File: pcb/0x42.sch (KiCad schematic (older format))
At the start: 26 parts, among them J1 USB_C_Receptacle_USB2.0, J2 ISP, Q1 2N7002, SW1 ~Reset, U1 ATmega32U4-MU, U2 PRTR5V0U2X, Y1 Crystal_GND24

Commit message: IS31 Led matrix
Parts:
- removed Q1: 2N7002, Package_TO_SOT_SMD:SOT-23, symbol Transistor_FET:2N7002
- removed R8: 100, 0xLib_Passive_SMD:R_0603_1608Metric, symbol Device:R
- removed R9: 10k, 0xLib_Passive_SMD:R_0603_1608Metric, symbol Device:R
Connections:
- net labels added: SCL, SDA
- net labels removed: LED_GND, LED_PWM
- wire segments 172 -> 164
- no-connect marks 8 -> 7
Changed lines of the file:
@@
 F1 "leds.sch" 50
 F2 "LED_DIN" I L 8900 3950 50
-F3 "LED_GND" I L 8900 4100 50
 $EndSheet
 Wire Wire Line
@@
 Wire Wire Line
 	6900 2700 6650 2700
-Wire Wire Line
-	6650 2600 7100 2600
-$Comp
-L Device:R R8
-U 1 1 5EB8CFA0
-P 7250 2600
-F 0 "R8" V 7150 2600 50  0000 C CNN
-F 1 "100" V 7250 2600 50  0000 C CNN
-F 2 "0xLib_Passive_SMD:R_0603_1608Metric" V 7180 2600 50  0001 C CNN
-F 3 "~" H 7250 2600 50  0001 C CNN
-	1    7250 2600
-	0    1    1    0
-$EndComp
-$Comp
-L Transistor_FET:2N7002 Q1
-U 1 1 5EB8E756
-P 7700 2600
-F 0 "Q1" H 7904 2646 50  0000 L CNN
-F 1 "2N7002" H 7904 2555 50  0000 L CNN
-F 2 "Package_TO_SOT_SMD:SOT-23" H 7900 2525 50  0001 L CIN
-F 3 "https://www.fairchildsemi.com/datasheets/2N/2N7002.pdf" H 7700 2600 50  0001 L CNN
-	1    7700 2600
-	1    0    0    -1
-$EndComp
-$Comp
-L power:GND #PWR0105
-U 1 1 5EB9C6F9
-P 7800 3050
-F 0 "#PWR0105" H 7800 2800 50  0001 C CNN
-F 1 "GND" H 7805 2877 50  0000 C CNN
-F 2 "" H 7800 3050 50  0001 C CNN
-F 3 "" H 7800 3050 50  0001 C CNN
-	1    7800 3050
-	1    0    0    -1
-$EndComp
-Text GLabel 8550 4100 0    50   Input ~ 0
-LED_GND
-Wire Wire Line
-	7800 2400 7800 2300
-Text GLabel 7800 2300 1    50   Input ~ 0
-LED_GND
 Wire Wire Line
 	2050 2950 3100 2950
@@
 Text Label 2550 2950 0    50   ~ 0
 BUS_D+
-Text Label 6700 2600 0    50   ~ 0
-LED_PWM
 Text Label 6900 1350 0    50   ~ 0
 MISO
@@
 	1350 3750 1350 3850
 Wire Wire Line
-	7400 2600 7450 2600
-Wire Wire Line
-	7800 2800 7800 3000
-Wire Wire Line
 	1050 3750 1050 3800
 $Comp
@@
 Wire Wire Line
 	6900 3400 6650 3400
-$Comp
-L Device:R R9
-U 1 1 5FAAAD36
-P 7450 2800
-F 0 "R9" V 7350 2800 50  0000 C CNN
-F 1 "10k" V 7450 2800 50  0000 C CNN
-F 2 "0xLib_Passive_SMD:R_0603_1608Metric" V 7380 2800 50  0001 C CNN
-F 3 "~" H 7450 2800 50  0001 C CNN
-	1    7450 2800
-	-1   0    0    1
-$EndComp
-Wire Wire Line
-	7450 2650 7450 2600
-Connection ~ 7450 2600
-Wire Wire Line
-	7450 2600 7500 2600
-Wire Wire Line
-	7450 2950 7450 3000
-Wire Wire Line
-	7450 3000 7800 3000
-Connection ~ 7800 3000
-Wire Wire Line
-	7800 3050 7800 3000
 Text GLabel 1050 3800 3    50   Input ~ 0
 Shield
-NoConn ~ 6650 2900
-NoConn ~ 6650 3000
 $Comp
 L Device:C C16
@@
 Wire Wire Line
 	10300 1300 10050 1300
-Wire Wire Line
-	8550 4100 8900 4100
 Text GLabel 6900 3100 2    50   Input ~ 0
 Col13
+Wire Wire Line
+	6650 3000 6900 3000
+Wire Wire Line
+	6650 2900 6900 2900
+Text GLabel 6900 3000 2    50   Input ~ 0
+SDA
+Text GLabel 6900 2900 2    50   Input ~ 0
+SCL
+NoConn ~ 6650 2600
 $EndSCHEMATC

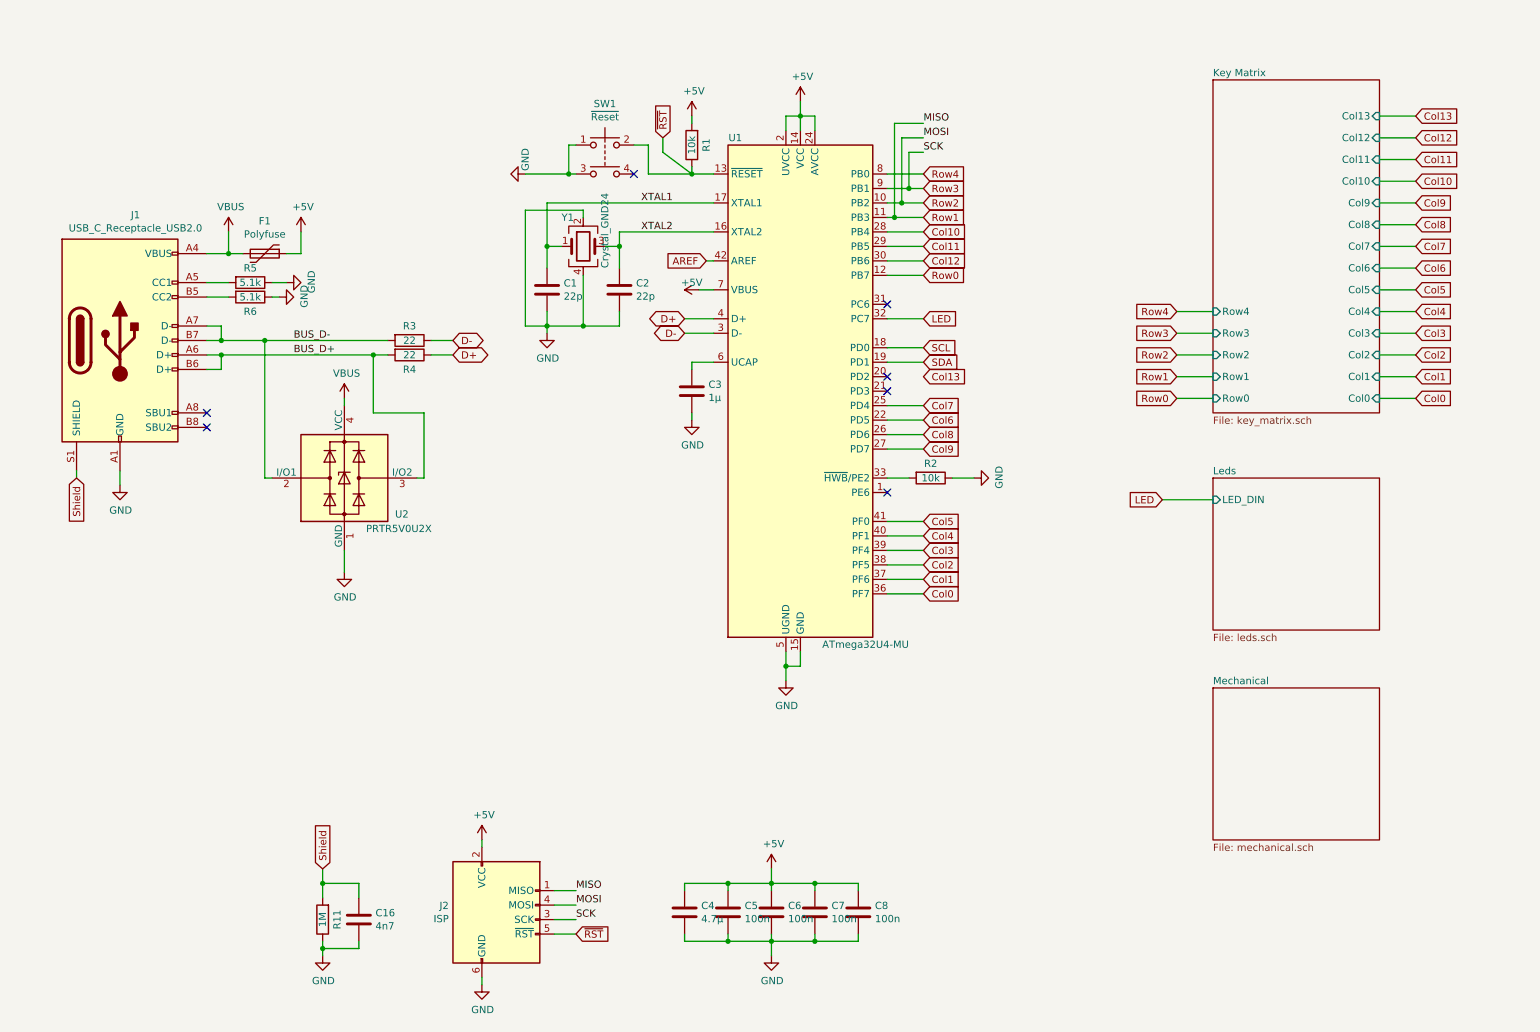
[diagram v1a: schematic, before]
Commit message: Start conversion to stm32
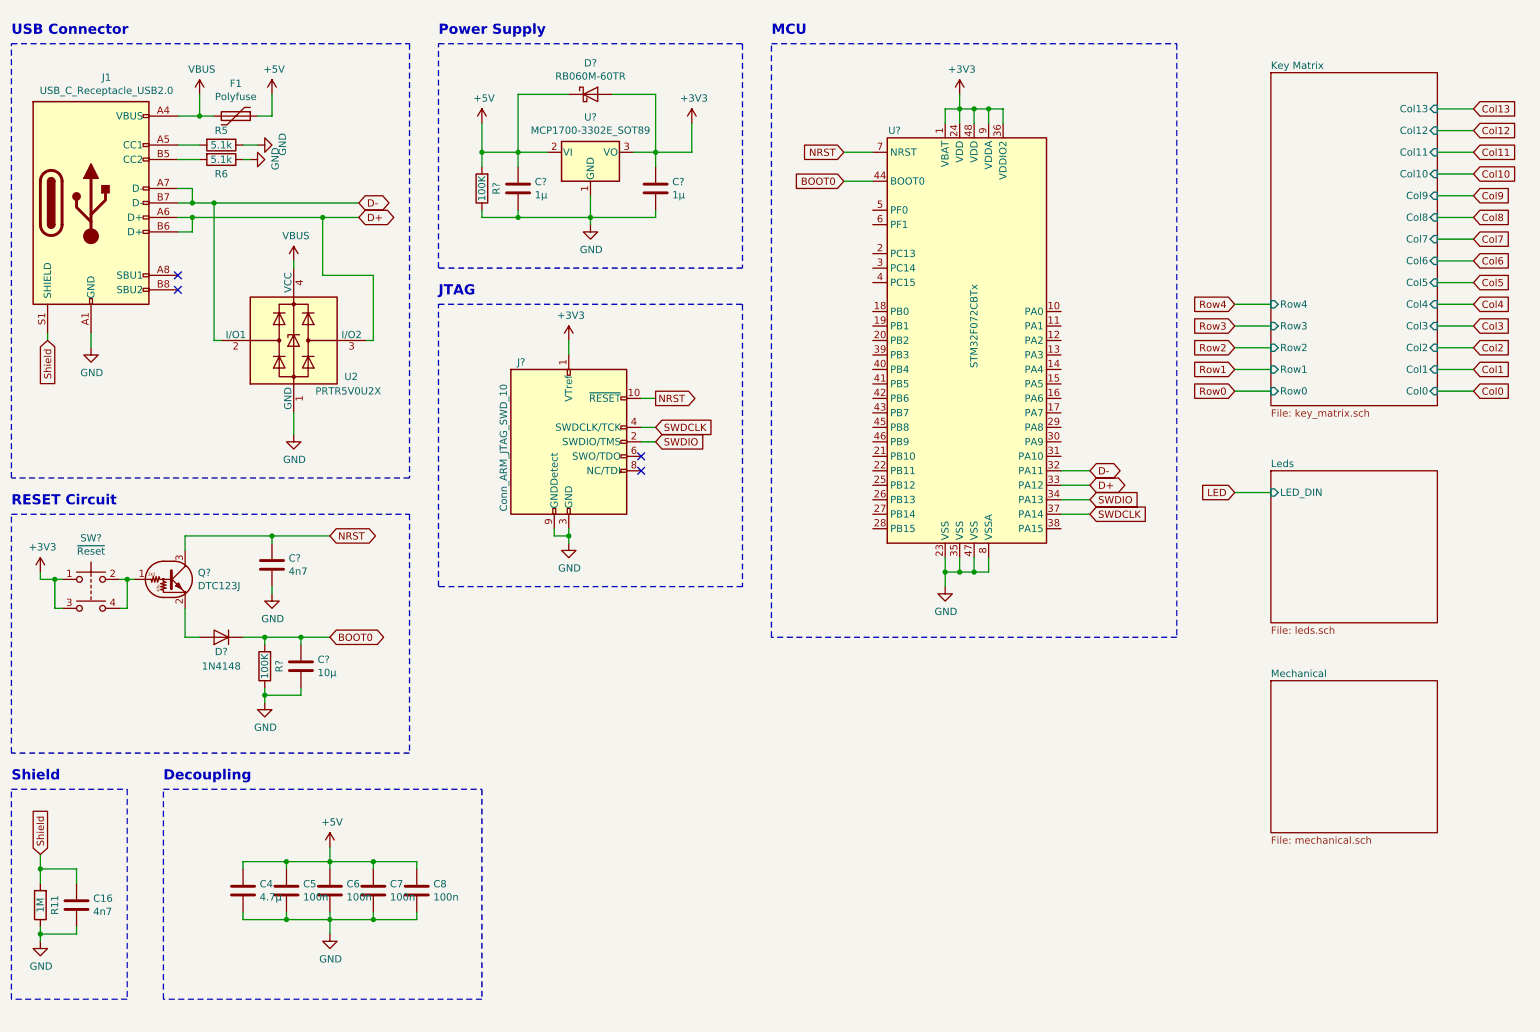
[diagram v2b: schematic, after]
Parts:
- removed C1, C2: 22p, 0xLib_Passive_SMD:C_0603_1608Metric, symbol Device:C
- removed C3: 1µ, 0xLib_Passive_SMD:C_0603_1608Metric, symbol Device:C
- removed J2: ISP, 0xLib_AVR:ISP_2x03_P2.54mm_Vertical, symbol Connector:AVR-ISP-6
- removed R1, R2: 10k, 0xLib_Passive_SMD:R_0603_1608Metric, symbol Device:R
- removed R3, R4: 22, 0xLib_Passive_SMD:R_0603_1608Metric, symbol Device:R
- removed SW1: ~Reset, 0xLib_Switch_Button:TACT_SWITCH_5.2x5.2_4Pin, symbol Switch:SW_Push_Dual
- removed U1: ATmega32U4-MU, Package_DFN_QFN:QFN-44-1EP_7x7mm_P0.5mm_EP5.2x5.2mm, symbol MCU_Microchip_ATmega:ATmega32U4-MU
- removed Y1: Crystal_GND24, Crystal:Crystal_SMD_SeikoEpson_FA238-4Pin_3.2x2.5mm, symbol Device:Crystal_GND24
- added C?: 4n7, 0xLib_Passive_SMD:C_0603_1608Metric, symbol Device:C
- added C?: 10µ, 0xLib_Passive_SMD:C_0603_1608Metric, symbol Device:C
- added C? (x2): 1µ, 0xLib_Passive_SMD:C_0603_1608Metric, symbol Device:C
- added D?: 1N4148, Diode_THT:D_DO-35_SOD27_P7.62mm_Horizontal, symbol Diode:1N4148
- added D?: RB060M-60TR, symbol Device:D_Schottky
- added J?: Conn_ARM_JTAG_SWD_10, symbol Connector:Conn_ARM_JTAG_SWD_10
- added Q?: DTC123J, symbol Transistor_BJT:DTC123J
- added R? (x2): 100K, 0xLib_Passive_SMD:R_0603_1608Metric, symbol Device:R
- added SW?: ~Reset, 0xLib_Switch_Button:TACT_SWITCH_5.2x5.2_4Pin, symbol Switch:SW_Push_Dual
- added U?: STM32F072CBTx, Package_QFP:LQFP-48_7x7mm_P0.5mm, symbol MCU_ST_STM32F0:STM32F072CBTx
- added U?: MCP1700-3302E_SOT89, Package_TO_SOT_SMD:SOT-89-3, symbol Regulator_Linear:MCP1700-3302E_SOT89
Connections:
- net BUS_D+ is gone; now on net D+: J1.A6 (D+), J1.B6 (D+), U2.3 (I/O2)
- net BUS_D- is gone; now on net D-: J1.A7 (D-), J1.B7 (D-), U2.2 (I/O1)
- net +5V: now also C?.1, D?.1 (K), R?.2, U?.2 (VI)
- net D+: now also U?.33 (PA12)
- net D-: now also U?.32 (PA11)
- net GND: now also C?.2, C?.2, C?.2, C?.2, J?.3 (GND), J?.5 (GND), J?.9 (GNDDetect), R?.1, R?.1, U?.1 (GND), U?.23 (VSS), U?.35 (VSS), U?.47 (VSS), U?.8 (VSSA)
- new net: Q?.1 (B), SW?.2, SW?.4
- new net: D?.2 (A), Q?.2 (E)
- new net +3V3: C?.1, D?.2 (A), J?.1 (VTref), SW?.1, SW?.3, U?.1 (VBAT), U?.24 (VDD), U?.3 (VO), U?.36 (VDDIO2), U?.48 (VDD), U?.9 (VDDA)
- new net BOOT0: C?.1, D?.1 (K), R?.2, U?.44 (BOOT0)
- new net NRST: C?.1, J?.10 (~RESET~), Q?.3 (C), U?.7 (NRST)
- new net SWDCLK: J?.4 (SWDCLK/TCK), U?.37 (PA14)
- new net SWDIO: J?.2 (SWDIO/TMS), U?.34 (PA13)
- no-connect marks 7 -> 4
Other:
- note added: "Decoupling"
- note added: "JTAG"
- note added: "MCU"
- note added: "Power Supply"
- note added: "RESET Circuit"
- note added: "Shield"
- note added: "USB Connector"
- moved on the sheet: C16, C4, C5, C6, C7, C8, F1, J1, R11, R5, R6, U2

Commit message: Complete STM32 PCB v1
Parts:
- removed D?: 1N4148, Diode_THT:D_DO-35_SOD27_P7.62mm_Horizontal, symbol Diode:1N4148
- removed D?: RB060M-60TR, symbol Device:D_Schottky
- removed Q?: DTC123J, symbol Transistor_BJT:DTC123J
- removed R?: 100K, 0xLib_Passive_SMD:R_0603_1608Metric, symbol Device:R
- removed U?: STM32F072CBTx, Package_QFP:LQFP-48_7x7mm_P0.5mm, symbol MCU_ST_STM32F0:STM32F072CBTx
- added C12, C13: 4µ7, 0xLib_Passive_SMD:C_0603_1608Metric, symbol Device:C
- added C5, C6: 10n, 0xLib_Passive_SMD:C_0603_1608Metric, symbol Device:C
- added Cb1: 4µ7, 0xLib_Passive_SMD:C_0805_2012Metric, symbol Device:C
- added J2: Conn_01x04, Connector_JST:JST_SH_SM04B-SRSS-TB_1x04-1MP_P1.00mm_Horizontal, symbol Connector_Generic:Conn_01x04
- added R4, R5, R6, R7: 10K, 0xLib_Passive_SMD:R_0603_1608Metric, symbol Device:R
- added SW2: Boot, 0xLib_Switch_Button:TACT_SWITCH_5.2x5.2_4Pin, symbol 0xLib_Switch_Button:SW_Push_4pin
- added U1: STM32F072CBUx, Package_DFN_QFN:QFN-48-1EP_7x7mm_P0.5mm_EP5.6x5.6mm, symbol MCU_ST_STM32F0:STM32F072CBUx
- C0: renamed from C16; footprint 0xLib_Passive_SMD:C_0603_1608Metric -> 0xLib_Passive_SMD:C_0805_2012Metric
- C1: renamed from C?; value 1µ -> 4µ7; footprint 0xLib_Passive_SMD:C_0603_1608Metric -> 0xLib_Passive_SMD:C_0805_2012Metric
- C11: renamed from C8; value 100n -> 1µ
- C3: renamed from C?; value 4n7 -> 100n
- C4: renamed from C?; value 10µ -> 100n
- C7: renamed from C4; value 4.7µ -> 10n; footprint 0xLib_Passive_SMD:C_1206_3216Metric -> 0xLib_Passive_SMD:C_0603_1608Metric
- J3: renamed from J?; value Conn_ARM_JTAG_SWD_10 -> SWD; footprint (none) -> 0xLib_STM32:ARM_JTAG_SWD_10
- R1: renamed from R?; value 100K -> 10K
- SW1: renamed from SW?; value ~Reset -> Reset; symbol Switch:SW_Push_Dual -> 0xLib_Switch_Button:SW_Push_4pin
- gave numbers to parts that had none: 2
- renumbered C7 to C10, C5 to C8, C6 to C9, U2 to D1, R11 to R0, R5 to R2, R6 to R3
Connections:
- net +3V3: now also C10.1, C11.1, C7.1, C8.1, C9.1, C12.1, C13.1, R4.2, R6.2, SW2.1, U1.1 (VBAT), U1.24 (VDD), U1.36 (VDDIO2), U1.48 (VDD), U1.9 (VDDA); no longer SW1.1, SW1.3
- net +5V: now also Cb1.1, J2.1 (Pin_1); no longer C10.1, C11.1, C7.1, C8.1, C9.1
- net BOOT0: now also SW2.4, U1.44 (BOOT0)
- net Col0: now also U1.12 (PA2)
- net Col1: now also U1.43 (PB7)
- net Col10: now also U1.25 (PB12)
- net Col11: now also U1.26 (PB13)
- net Col12: now also U1.27 (PB14)
- net Col13: now also U1.28 (PB15)
- net Col2: now also U1.42 (PB6)
- net Col3: now also U1.41 (PB5)
- net Col4: now also U1.40 (PB4)
- net Col5: now also U1.39 (PB3)
- net Col6: now also U1.38 (PA15)
- net Col7: now also U1.13 (PA3)
- net Col8: now also U1.14 (PA4)
- net Col9: now also U1.15 (PA5)
- net D+: now also J2.3 (Pin_3), U1.33 (PA12)
- net D-: now also J2.2 (Pin_2), U1.32 (PA11)
- net GND: now also SW1.1, C12.2, C13.2, C5.2, C6.2, Cb1.2, J2.4 (Pin_4), U1.23 (VSS), U1.35 (VSS), U1.47 (VSS), U1.49 (VSS), U1.8 (VSSA)
- net NRST: now also SW1.4, U1.7 (NRST)
- net Row0: now also U1.22 (PB11)
- net Row1: now also U1.21 (PB10)
- net Row2: now also U1.20 (PB2)
- net Row3: now also U1.19 (PB1)
- net Row4: now also U1.18 (PB0)
- net SWDCLK: now also U1.37 (PA14)
- net SWDIO: now also U1.34 (PA13)
- net at SW1.2: no longer SW1.4
- new net EncOut_A: C5.1, R5.1, U1.16 (PA6)
- new net EncOut_B: C6.1, R7.1, U1.17 (PA7)
- new net Enc_A: R4.1, R5.2
- new net Enc_B: R6.1, R7.2
- new net IS31_~SDB: U1.5 (PF0)
- new net SCL: U1.45 (PB8)
- new net SDA: U1.46 (PB9)
- no-connect marks 4 -> 13
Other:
- note added: "Encoder interface"
- note added: "MCU decoupling"
- note added: "Programming header"
- note added: "Reset/Boot switches"
- note added: "Shielding"
- note added: "USB connector"
- note added: "USB daughterboard"
- note added: "Voltage regulator"
- note removed: "Decoupling"
- note removed: "JTAG"
- note removed: "Power Supply"
- note removed: "RESET Circuit"
- note removed: "Shield"
- note removed: "USB Connector"
- moved on the sheet: C0, C1, C10, C11, C2, C3, C4, C7, C8, C9, D1, F1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

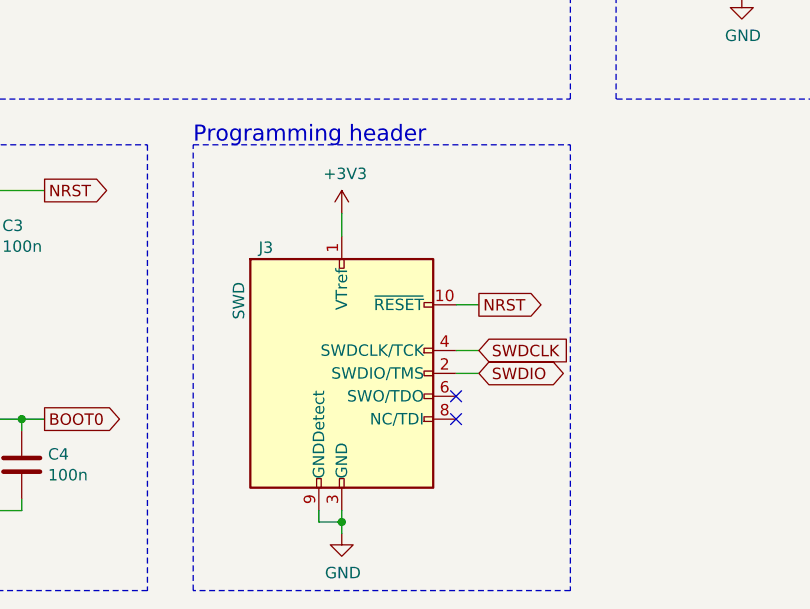
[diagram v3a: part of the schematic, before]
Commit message: Replace 2x05pins SWD connector by 1x06 (Nucleo CN4 pinout)
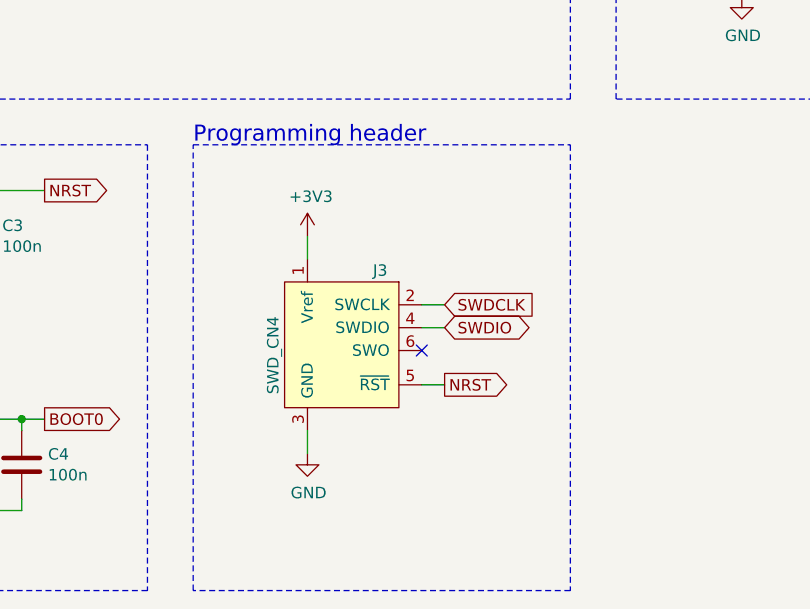
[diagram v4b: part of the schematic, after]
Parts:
- removed J3: SWD, 0xLib_STM32:ARM_JTAG_SWD_10, symbol Connector:Conn_ARM_JTAG_SWD_10
- added J3: SWD_CN4, 0xLib_STM32:SWD_1x06_P2.54mm_POGO, symbol 0xLib_STM32:SWD_CN4
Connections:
- net +3V3: now also J3.1 (Vref)
- net GND: now also J3.3 (GND)
- net NRST: now also J3.5 (~RST)
- net SWDCLK: now also J3.2 (SWCLK)
- net SWDIO: now also J3.4 (SWDIO)
- no-connect marks 13 -> 12
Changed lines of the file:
@@
 Wire Wire Line
 	10600 1650 10450 1650
-$Comp
-L Connector:Conn_ARM_JTAG_SWD_10 J3
-U 1 1 632C1AE9
-P 5550 6600
-F 0 "J3" H 5250 7150 50  0000 R CNN
-F 1 "SWD" V 5100 7000 50  0000 R CNN
-F 2 "0xLib_STM32:ARM_JTAG_SWD_10" H 5550 6600 50  0001 C CNN
-F 3 "http://infocenter.arm.com/help/topic/com.arm.doc.ddi0314h/DDI0314H_coresight_components_trm.pdf" V 5200 5350 50  0001 C CNN
-	1    5550 6600
-	1    0    0    -1
-$EndComp
 Text GLabel 950  2900 3    50   Input ~ 0
 Shield
@@
 L power:GND #PWR013
 U 1 1 6335C60E
-P 5550 7300
-F 0 "#PWR013" H 5550 7050 50  0001 C CNN
-F 1 "GND" H 5555 7127 50  0000 C CNN
-F 2 "" H 5550 7300 50  0001 C CNN
-F 3 "" H 5550 7300 50  0001 C CNN
-	1    5550 7300
-	1    0    0    -1
-$EndComp
-Wire Wire Line
-	5550 7300 5550 7250
-Wire Wire Line
-	5550 7250 5450 7250
-Wire Wire Line
-	5450 7250 5450 7200
-Connection ~ 5550 7250
-Wire Wire Line
-	5550 7250 5550 7200
+P 5400 6950
+F 0 "#PWR013" H 5400 6700 50  0001 C CNN
+F 1 "GND" H 5405 6777 50  0000 C CNN
+F 2 "" H 5400 6950 50  0001 C CNN
+F 3 "" H 5400 6950 50  0001 C CNN
+	1    5400 6950
+	1    0    0    -1
+$EndComp
 $Comp
 L power:+3V3 #PWR012
 U 1 1 63371FB0
-P 5550 5900
-F 0 "#PWR012" H 5550 5750 50  0001 C CNN
-F 1 "+3V3" H 5565 6073 50  0000 C CNN
-F 2 "" H 5550 5900 50  0001 C CNN
-F 3 "" H 5550 5900 50  0001 C CNN
-	1    5550 5900
-	1    0    0    -1
-$EndComp
-Wire Wire Line
-	5550 5900 5550 6000
-NoConn ~ 6050 6700
-NoConn ~ 6050 6800
-Wire Wire Line
-	6050 6300 6150 6300
-Wire Wire Line
-	6050 6500 6150 6500
-Wire Wire Line
-	6050 6600 6150 6600
-Text GLabel 6150 6300 2    50   Output ~ 0
+P 5400 6000
+F 0 "#PWR012" H 5400 5850 50  0001 C CNN
+F 1 "+3V3" H 5415 6173 50  0000 C CNN
+F 2 "" H 5400 6000 50  0001 C CNN
+F 3 "" H 5400 6000 50  0001 C CNN
+	1    5400 6000
+	1    0    0    -1
+$EndComp
+Wire Wire Line
+	5400 6000 5400 6100
+Wire Wire Line
+	5900 6650 6000 6650
+Wire Wire Line
+	5900 6300 6000 6300
+Wire Wire Line
+	5900 6400 6000 6400
+Text GLabel 6000 6650 2    50   Output ~ 0
 NRST
-Text GLabel 6150 6500 2    50   Input ~ 0
+Text GLabel 6000 6300 2    50   Input ~ 0
 SWDCLK
-Text GLabel 6150 6600 2    50   BiDi ~ 0
+Text GLabel 6000 6400 2    50   BiDi ~ 0
 SWDIO
 Wire Wire Line
@@
 NoConn ~ 4400 2500
 NoConn ~ 4400 2600
+$Comp
+L 0xLib_STM32:SWD_CN4 J3
+U 1 1 5F61B5B8
+P 5500 6400
+F 0 "J3" H 5750 6650 50  0000 R CNN
+F 1 "SWD_CN4" V 5250 6450 50  0000 R CNN
+F 2 "0xLib_STM32:SWD_1x06_P2.54mm_POGO" H 5500 6400 50  0001 C CNN
+F 3 "" H 5500 6400 50  0001 C CNN
+	1    5500 6400
+	1    0    0    -1
+$EndComp
+Wire Wire Line
+	5400 6850 5400 6950
+NoConn ~ 5900 6500
 $EndSCHEMATC
